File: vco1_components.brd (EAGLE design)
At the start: 106 x 50 mm, 59 parts, among them IC1 LM13700N, Q3 2N3904, Q4 2N3904, U1 TL072_, U2 TL072_, U3 TL072_

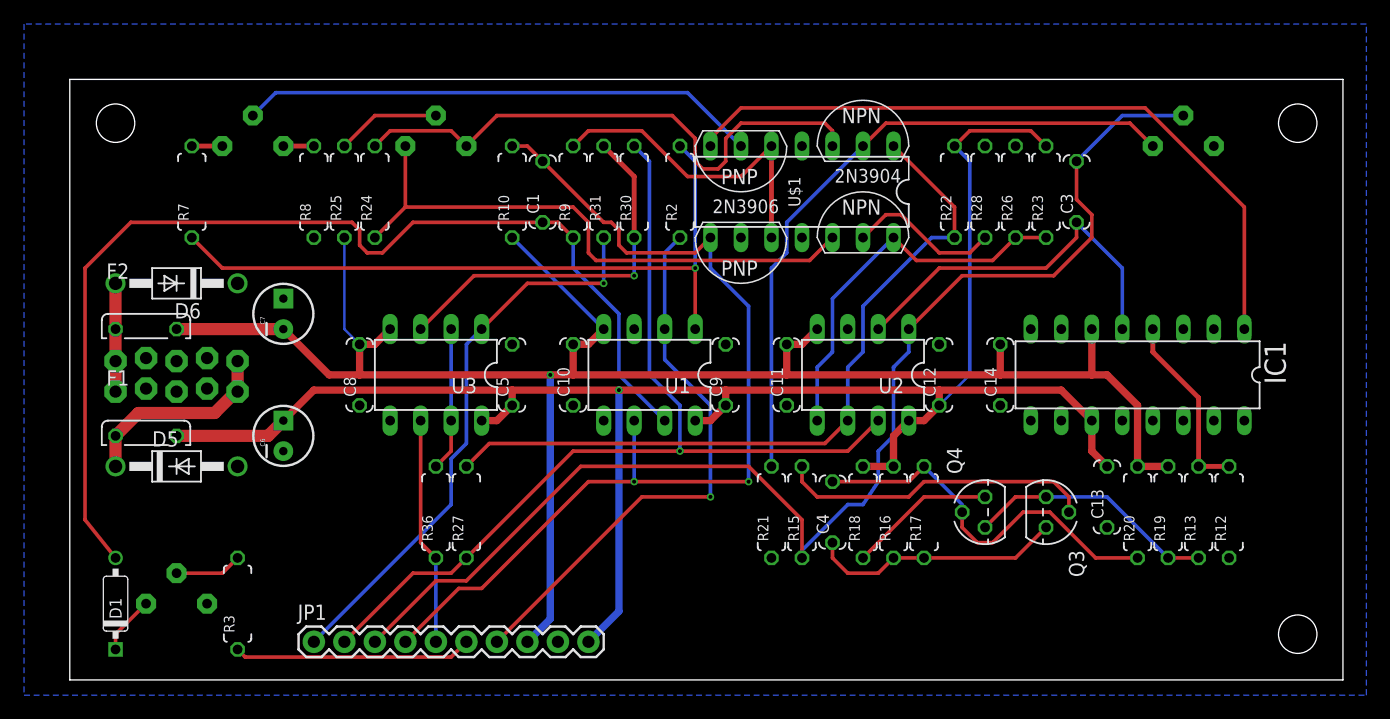
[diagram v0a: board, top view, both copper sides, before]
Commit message: Make trimpot accessible from side
...when side-trimmable trimpot ist used.
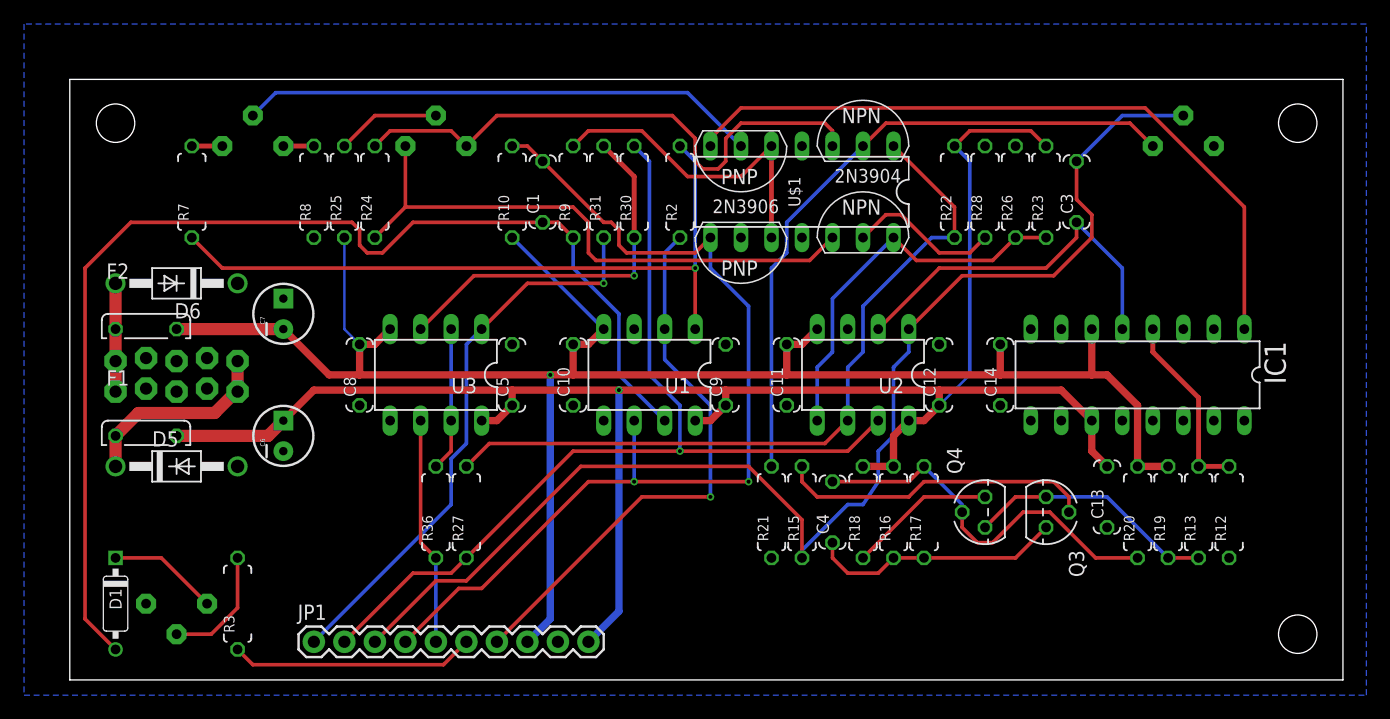
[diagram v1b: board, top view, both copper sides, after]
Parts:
- R10: value 1.2m -> 1.2M
- R3: value 2.2m -> 2.2M
- turned D1 to 270 degrees
- turned HIGH_FREQ_TRIM to 180 degrees
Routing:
- net N$13: track 89.0 -> 96.8 mm
- net N$16: track 5.61 -> 10.1 mm
- net N$15: track 4.86 -> 9.20 mm
- net CV_B: track 19.8 -> 20.4 mm
